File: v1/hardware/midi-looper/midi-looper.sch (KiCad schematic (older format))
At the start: 19 parts

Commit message: Updated schematic
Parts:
- added R? (x3): 10, symbol Device:R
- added R? (x3): 33, symbol Device:R
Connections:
- net +3V3: now also R?.1, R?.1, R?.1
- net GND: now also J?.2 (Pin_2), J?.2 (Pin_2), J?.2 (Pin_2)
- net TX3: now reaches U?.10 (8_TX3_DIN)
- net TX3: now also R?.2
- net TX2: now reaches U?.12 (10_TX2_CS_PWM)
- net TX2: now also R?.2
- net TX1: now reaches U?.3 (1_TX1_Touch)
- net TX1: now also R?.2
- net at J?.1 (Pin_1): now also R?.1 (x3)
- net at J?.3 (Pin_3): now also R?.2 (x3)
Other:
- moved on the sheet: J?
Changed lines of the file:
@@
 L Connector:Conn_01x03_Female J?
 U 1 1 61B8E575
-P 3950 1000
-F 0 "J?" V 3888 812 50  0000 R CNN
-F 1 "Conn_01x03_Female" V 3797 812 50  0000 R CNN
-F 2 "" H 3950 1000 50  0001 C CNN
-F 3 "~" H 3950 1000 50  0001 C CNN
-	1    3950 1000
+P 7550 1400
+F 0 "J?" V 7488 1212 50  0000 R CNN
+F 1 "Conn_01x03_Female" V 7397 1212 50  0000 R CNN
+F 2 "" H 7550 1400 50  0001 C CNN
+F 3 "~" H 7550 1400 50  0001 C CNN
+	1    7550 1400
 	0    -1   -1   0
 $EndComp
@@
 L Connector:Conn_01x03_Female J?
 U 1 1 61B91527
-P 4900 1000
-F 0 "J?" V 4838 812 50  0000 R CNN
-F 1 "Conn_01x03_Female" V 4747 812 50  0000 R CNN
-F 2 "" H 4900 1000 50  0001 C CNN
-F 3 "~" H 4900 1000 50  0001 C CNN
-	1    4900 1000
+P 8500 1400
+F 0 "J?" V 8438 1212 50  0000 R CNN
+F 1 "Conn_01x03_Female" V 8347 1212 50  0000 R CNN
+F 2 "" H 8500 1400 50  0001 C CNN
+F 3 "~" H 8500 1400 50  0001 C CNN
+	1    8500 1400
 	0    -1   -1   0
 $EndComp
@@
 L Connector:Conn_01x03_Female J?
 U 1 1 61B91E09
-P 5850 1000
-F 0 "J?" V 5788 812 50  0000 R CNN
-F 1 "Conn_01x03_Female" V 5697 812 50  0000 R CNN
-F 2 "" H 5850 1000 50  0001 C CNN
-F 3 "~" H 5850 1000 50  0001 C CNN
-	1    5850 1000
+P 9450 1400
+F 0 "J?" V 9388 1212 50  0000 R CNN
+F 1 "Conn_01x03_Female" V 9297 1212 50  0000 R CNN
+F 2 "" H 9450 1400 50  0001 C CNN
+F 3 "~" H 9450 1400 50  0001 C CNN
+	1    9450 1400
 	0    -1   -1   0
 $EndComp
+$Comp
+L Device:R R?
+U 1 1 61B9C710
+P 7450 1750
+F 0 "R?" H 7520 1796 50  0000 L CNN
+F 1 "10" H 7520 1705 50  0000 L CNN
+F 2 "" V 7380 1750 50  0001 C CNN
+F 3 "~" H 7450 1750 50  0001 C CNN
+	1    7450 1750
+	1    0    0    -1
+$EndComp
+$Comp
+L Device:R R?
+U 1 1 61B9D0B4
+P 8400 1750
+F 0 "R?" H 8470 1796 50  0000 L CNN
+F 1 "10" H 8470 1705 50  0000 L CNN
+F 2 "" V 8330 1750 50  0001 C CNN
+F 3 "~" H 8400 1750 50  0001 C CNN
+	1    8400 1750
+	1    0    0    -1
+$EndComp
+$Comp
+L Device:R R?
+U 1 1 61B9D95C
+P 9350 1750
+F 0 "R?" H 9420 1796 50  0000 L CNN
+F 1 "10" H 9420 1705 50  0000 L CNN
+F 2 "" V 9280 1750 50  0001 C CNN
+F 3 "~" H 9350 1750 50  0001 C CNN
+	1    9350 1750
+	1    0    0    -1
+$EndComp
+Text Label 7450 1900 0    50   ~ 0
+TX1
+Text Label 8400 1900 0    50   ~ 0
+TX2
+Text Label 9350 1900 0    50   ~ 0
+TX3
+Text Label 6000 3950 0    50   ~ 0
+TX1
+Text Label 5100 3950 0    50   ~ 0
+TX2
+Text Label 5300 3950 0    50   ~ 0
+TX3
+$Comp
+L power:GND #PWR?
+U 1 1 61BA81F2
+P 7550 2000
+F 0 "#PWR?" H 7550 1750 50  0001 C CNN
+F 1 "GND" H 7555 1827 50  0000 C CNN
+F 2 "" H 7550 2000 50  0001 C CNN
+F 3 "" H 7550 2000 50  0001 C CNN
+	1    7550 2000
+	1    0    0    -1
+$EndComp
+$Comp
+L power:GND #PWR?
+U 1 1 61BA87AF
+P 8500 1950
+F 0 "#PWR?" H 8500 1700 50  0001 C CNN
+F 1 "GND" H 8505 1777 50  0000 C CNN
+F 2 "" H 8500 1950 50  0001 C CNN
+F 3 "" H 8500 1950 50  0001 C CNN
+	1    8500 1950
+	1    0    0    -1
+$EndComp
+$Comp
+L power:GND #PWR?
+U 1 1 61BA8AF1
+P 9450 1950
+F 0 "#PWR?" H 9450 1700 50  0001 C CNN
+F 1 "GND" H 9455 1777 50  0000 C CNN
+F 2 "" H 9450 1950 50  0001 C CNN
+F 3 "" H 9450 1950 50  0001 C CNN
+	1    9450 1950
+	1    0    0    -1
+$EndComp
+Wire Wire Line
+	9450 1600 9450 1950
+Wire Wire Line
+	8500 1600 8500 1950
+Wire Wire Line
+	7550 2000 7550 1600
+$Comp
+L Device:R R?
+U 1 1 61BAD6A1
+P 9700 1600
+F 0 "R?" V 9493 1600 50  0000 C CNN
+F 1 "33" V 9584 1600 50  0000 C CNN
+F 2 "" V 9630 1600 50  0001 C CNN
+F 3 "~" H 9700 1600 50  0001 C CNN
+	1    9700 1600
+	0    1    1    0
+$EndComp
+$Comp
+L Device:R R?
+U 1 1 61BADCD9
+P 8750 1600
+F 0 "R?" V 8543 1600 50  0000 C CNN
+F 1 "33" V 8634 1600 50  0000 C CNN
+F 2 "" V 8680 1600 50  0001 C CNN
+F 3 "~" H 8750 1600 50  0001 C CNN
+	1    8750 1600
+	0    1    1    0
+$EndComp
+$Comp
+L Device:R R?
+U 1 1 61BAE254
+P 7800 1600
+F 0 "R?" V 7593 1600 50  0000 C CNN
+F 1 "33" V 7684 1600 50  0000 C CNN
+F 2 "" V 7730 1600 50  0001 C CNN
+F 3 "~" H 7800 1600 50  0001 C CNN
+	1    7800 1600
+	0    1    1    0
+$EndComp
+$Comp
+L power:+3.3V #PWR?
+U 1 1 61BAEFCC
+P 9850 1600
+F 0 "#PWR?" H 9850 1450 50  0001 C CNN
+F 1 "+3.3V" V 9865 1728 50  0000 L CNN
+F 2 "" H 9850 1600 50  0001 C CNN
+F 3 "" H 9850 1600 50  0001 C CNN
+	1    9850 1600
+	0    1    1    0
+$EndComp
+$Comp
+L power:+3.3V #PWR?
+U 1 1 61BAF8B9
+P 8900 1600
+F 0 "#PWR?" H 8900 1450 50  0001 C CNN
+F 1 "+3.3V" V 8915 1728 50  0000 L CNN
+F 2 "" H 8900 1600 50  0001 C CNN
+F 3 "" H 8900 1600 50  0001 C CNN
+	1    8900 1600
+	0    1    1    0
+$EndComp
+$Comp
+L power:+3.3V #PWR?
+U 1 1 61BAFE97
+P 7950 1600
+F 0 "#PWR?" H 7950 1450 50  0001 C CNN
+F 1 "+3.3V" V 7965 1728 50  0000 L CNN
+F 2 "" H 7950 1600 50  0001 C CNN
+F 3 "" H 7950 1600 50  0001 C CNN
+	1    7950 1600
+	0    1    1    0
+$EndComp
 $EndSCHEMATC

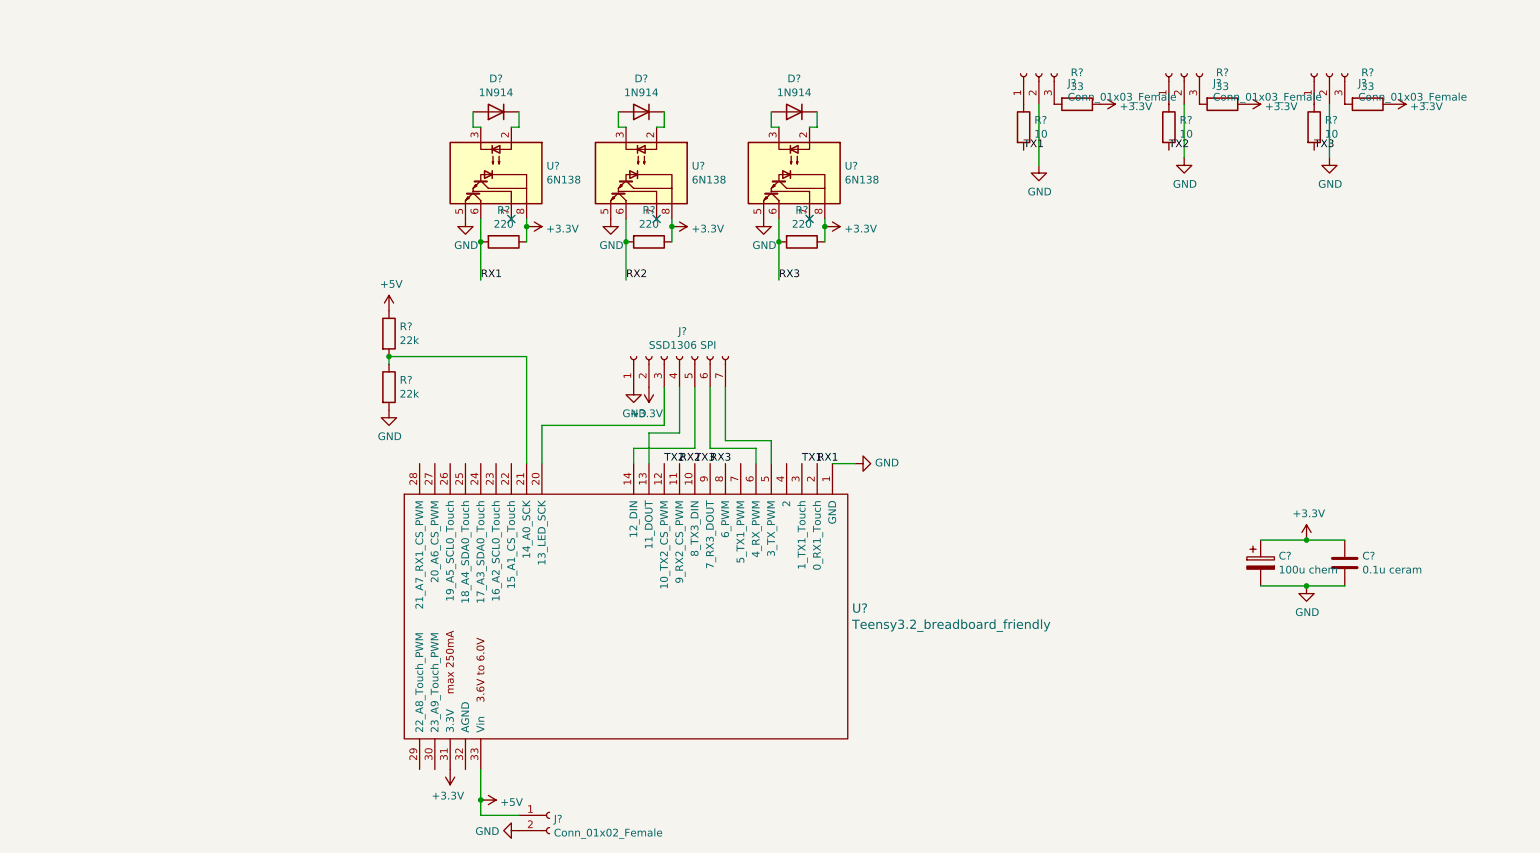
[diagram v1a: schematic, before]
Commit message: Complete initial schematic
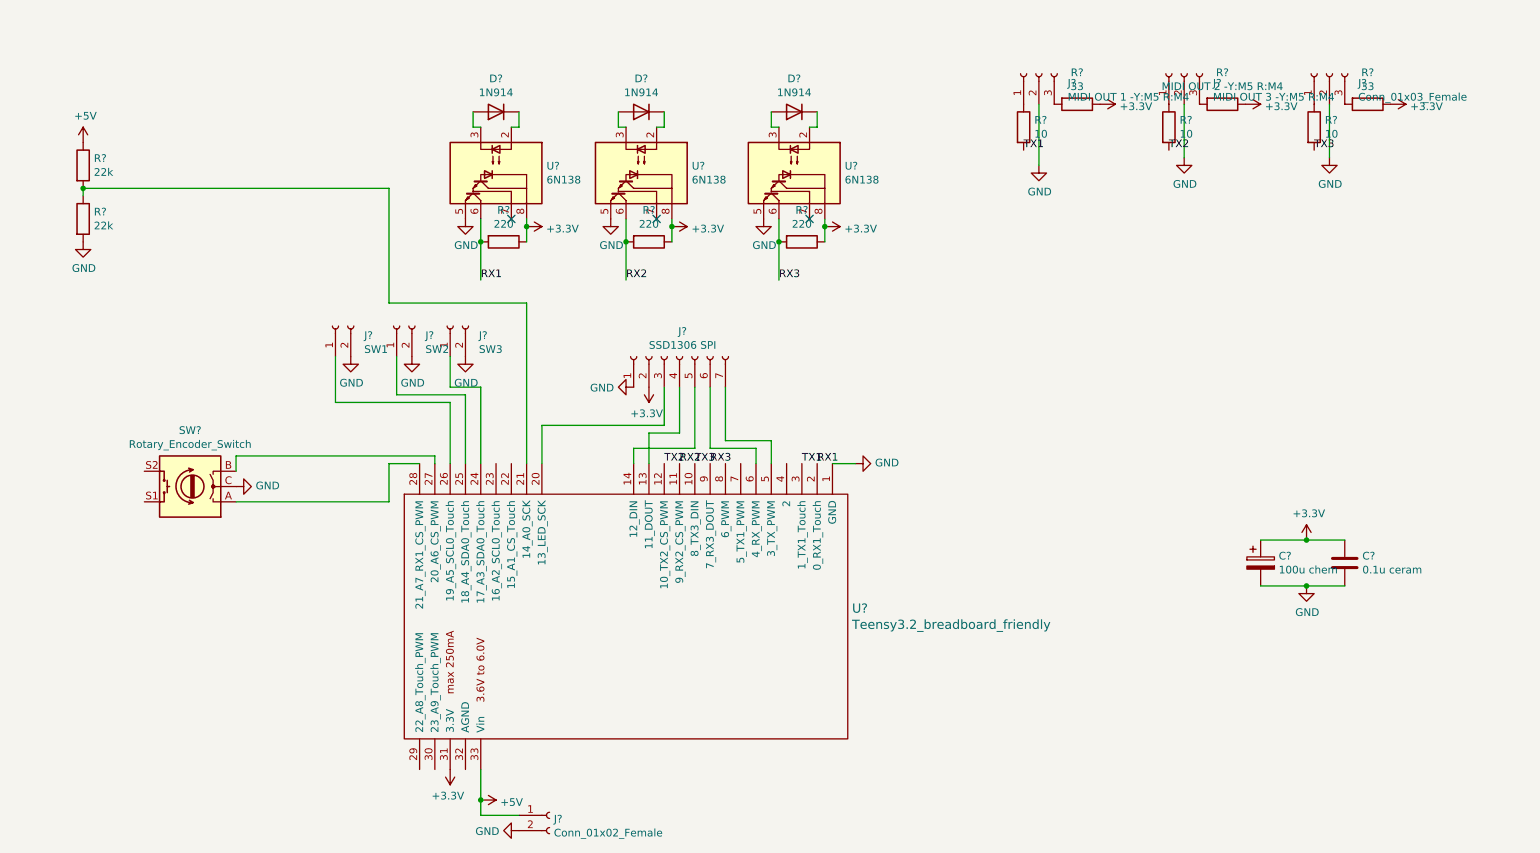
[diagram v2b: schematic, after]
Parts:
- added J?: SW1, symbol Connector:Conn_01x02_Female
- added J?: SW2, symbol Connector:Conn_01x02_Female
- added J?: SW3, symbol Connector:Conn_01x02_Female
- added SW?: Rotary_Encoder_Switch, symbol Device:Rotary_Encoder_Switch
- J?: value Conn_01x03_Female -> MIDI OUT 1 -Y:M5 R:M4
- J?: value Conn_01x03_Female -> MIDI OUT 3 -Y:M5 R:M4
- R?: value 33 -> MIDI OUT 2 -Y:M5 R:M4
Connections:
- net GND: now also J?.2 (Pin_2), J?.2 (Pin_2), J?.2 (Pin_2), SW?.C
- net at U?.24 (17_A3_SDA0_Touch): now also J?.1 (Pin_1)
- net at U?.25 (18_A4_SDA0_Touch): now also J?.1 (Pin_1)
- net at U?.26 (19_A5_SCL0_Touch): now also J?.1 (Pin_1)
- net at U?.27 (20_A6_CS_PWM): now also SW?.B
- net at U?.28 (21_A7_RX1_CS_PWM): now also SW?.A
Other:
- moved on the sheet: R?
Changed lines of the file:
@@
 P 4900 3450
 F 0 "#PWR?" H 4900 3200 50  0001 C CNN
-F 1 "GND" H 4905 3277 50  0000 C CNN
+F 1 "GND" V 4905 3322 50  0000 R CNN
 F 2 "" H 4900 3450 50  0001 C CNN
 F 3 "" H 4900 3450 50  0001 C CNN
 	1    4900 3450
-	1    0    0    -1
+	0    1    1    0
 $EndComp
 $Comp
@@
 	-1   0    0    1
 $EndComp
-Wire Wire Line
-	9000 4450 9300 4450
 $Comp
 L power:+5V #PWR?
 U 1 1 61B75368
-P 3300 2950
-F 0 "#PWR?" H 3300 2800 50  0001 C CNN
-F 1 "+5V" H 3315 3123 50  0000 C CNN
-F 2 "" H 3300 2950 50  0001 C CNN
-F 3 "" H 3300 2950 50  0001 C CNN
-	1    3300 2950
+P 1300 1850
+F 0 "#PWR?" H 1300 1700 50  0001 C CNN
+F 1 "+5V" H 1315 2023 50  0000 C CNN
+F 2 "" H 1300 1850 50  0001 C CNN
+F 3 "" H 1300 1850 50  0001 C CNN
+	1    1300 1850
 	1    0    0    -1
 $EndComp
@@
 L Device:R R?
 U 1 1 61B75E1A
-P 3300 3100
-F 0 "R?" H 3370 3146 50  0000 L CNN
-F 1 "22k" H 3370 3055 50  0000 L CNN
-F 2 "" V 3230 3100 50  0001 C CNN
-F 3 "~" H 3300 3100 50  0001 C CNN
-	1    3300 3100
+P 1300 2000
+F 0 "R?" H 1370 2046 50  0000 L CNN
+F 1 "22k" H 1370 1955 50  0000 L CNN
+F 2 "" V 1230 2000 50  0001 C CNN
+F 3 "~" H 1300 2000 50  0001 C CNN
+	1    1300 2000
 	1    0    0    -1
 $EndComp
@@
 L Device:R R?
 U 1 1 61B7670C
-P 3300 3450
-F 0 "R?" H 3370 3496 50  0000 L CNN
-F 1 "22k" H 3370 3405 50  0000 L CNN
-F 2 "" V 3230 3450 50  0001 C CNN
-F 3 "~" H 3300 3450 50  0001 C CNN
-	1    3300 3450
+P 1300 2350
+F 0 "R?" H 1370 2396 50  0000 L CNN
+F 1 "22k" H 1370 2305 50  0000 L CNN
+F 2 "" V 1230 2350 50  0001 C CNN
+F 3 "~" H 1300 2350 50  0001 C CNN
+	1    1300 2350
 	1    0    0    -1
 $EndComp
@@
 L power:GND #PWR?
 U 1 1 61B76E07
-P 3300 3600
-F 0 "#PWR?" H 3300 3350 50  0001 C CNN
-F 1 "GND" H 3305 3427 50  0000 C CNN
-F 2 "" H 3300 3600 50  0001 C CNN
-F 3 "" H 3300 3600 50  0001 C CNN
-	1    3300 3600
-	1    0    0    -1
-$EndComp
-Wire Wire Line
-	3300 3250 3300 3300
-Wire Wire Line
-	4200 3950 4200 3250
-Wire Wire Line
-	4200 3250 3300 3250
-Connection ~ 3300 3250
+P 1300 2500
+F 0 "#PWR?" H 1300 2250 50  0001 C CNN
+F 1 "GND" H 1305 2327 50  0000 C CNN
+F 2 "" H 1300 2500 50  0001 C CNN
+F 3 "" H 1300 2500 50  0001 C CNN
+	1    1300 2500
+	1    0    0    -1
+$EndComp
+Wire Wire Line
+	1300 2150 1300 2200
+Connection ~ 1300 2150
 $Comp
 L Connector:Conn_01x03_Female J?
@@
 P 7550 1400
 F 0 "J?" V 7488 1212 50  0000 R CNN
-F 1 "Conn_01x03_Female" V 7397 1212 50  0000 R CNN
+F 1 "MIDI OUT 1 -Y:M5 R:M4" V 7397 1212 50  0000 R CNN
 F 2 "" H 7550 1400 50  0001 C CNN
 F 3 "~" H 7550 1400 50  0001 C CNN
@@
 P 8500 1400
 F 0 "J?" V 8438 1212 50  0000 R CNN
-F 1 "Conn_01x03_Female" V 8347 1212 50  0000 R CNN
+F 1 "MIDI OUT 3 -Y:M5 R:M4" V 8347 1212 50  0000 R CNN
 F 2 "" H 8500 1400 50  0001 C CNN
 F 3 "~" H 8500 1400 50  0001 C CNN
@@
 P 8750 1600
 F 0 "R?" V 8543 1600 50  0000 C CNN
-F 1 "33" V 8634 1600 50  0000 C CNN
+F 1 "MIDI OUT 2 -Y:M5 R:M4" V 8634 1600 50  0000 C CNN
 F 2 "" V 8680 1600 50  0001 C CNN
 F 3 "~" H 8750 1600 50  0001 C CNN
@@
 	0    1    1    0
 $EndComp
+Wire Wire Line
+	9000 4450 9300 4450
+$Comp
+L Device:Rotary_Encoder_Switch SW?
+U 1 1 61BBEB55
+P 2000 4100
+F 0 "SW?" H 2000 3733 50  0000 C CNN
+F 1 "Rotary_Encoder_Switch" H 2000 3824 50  0000 C CNN
+F 2 "" H 1850 4260 50  0001 C CNN
+F 3 "~" H 2000 4360 50  0001 C CNN
+	1    2000 4100
+	-1   0    0    1
+$EndComp
+$Comp
+L power:GND #PWR?
+U 1 1 61BC1206
+P 2300 4100
+F 0 "#PWR?" H 2300 3850 50  0001 C CNN
+F 1 "GND" V 2305 3972 50  0000 R CNN
+F 2 "" H 2300 4100 50  0001 C CNN
+F 3 "" H 2300 4100 50  0001 C CNN
+	1    2300 4100
+	0    -1   -1   0
+$EndComp
+Wire Wire Line
+	2300 4200 3300 4200
+Wire Wire Line
+	3300 4200 3300 3950
+Wire Wire Line
+	3300 3950 3500 3950
+Wire Wire Line
+	3600 3950 3600 3900
+Wire Wire Line
+	3600 3900 2300 3900
+Wire Wire Line
+	2300 3900 2300 4000
+Wire Wire Line
+	4200 2900 3300 2900
+Wire Wire Line
+	3300 2900 3300 2150
+Wire Wire Line
+	4200 2900 4200 3950
+Wire Wire Line
+	1300 2150 3300 2150
+$Comp
+L Connector:Conn_01x02_Female J?
+U 1 1 61BDE879
+P 2950 3050
+F 0 "J?" V 2888 2862 50  0000 R CNN
+F 1 "SW1" V 2797 2862 50  0000 R CNN
+F 2 "" H 2950 3050 50  0001 C CNN
+F 3 "~" H 2950 3050 50  0001 C CNN
+	1    2950 3050
+	0    -1   -1   0
+$EndComp
+$Comp
+L Connector:Conn_01x02_Female J?
+U 1 1 61BDF6EB
+P 3350 3050
+F 0 "J?" V 3288 2862 50  0000 R CNN
+F 1 "SW2" V 3197 2862 50  0000 R CNN
+F 2 "" H 3350 3050 50  0001 C CNN
+F 3 "~" H 3350 3050 50  0001 C CNN
+	1    3350 3050
+	0    -1   -1   0
+$EndComp
+$Comp
+L Connector:Conn_01x02_Female J?
+U 1 1 61BE0034
+P 3700 3050
+F 0 "J?" V 3638 2862 50  0000 R CNN
+F 1 "SW3" V 3547 2862 50  0000 R CNN
+F 2 "" H 3700 3050 50  0001 C CNN
+F 3 "~" H 3700 3050 50  0001 C CNN
+	1    3700 3050
+	0    -1   -1   0
+$EndComp
+$Comp
+L power:GND #PWR?
+U 1 1 61BE421A
+P 3050 3250
+F 0 "#PWR?" H 3050 3000 50  0001 C CNN
+F 1 "GND" H 3055 3077 50  0000 C CNN
+F 2 "" H 3050 3250 50  0001 C CNN
+F 3 "" H 3050 3250 50  0001 C CNN
+	1    3050 3250
+	1    0    0    -1
+$EndComp
+$Comp
+L power:GND #PWR?
+U 1 1 61BE4AA7
+P 3450 3250
+F 0 "#PWR?" H 3450 3000 50  0001 C CNN
+F 1 "GND" H 3455 3077 50  0000 C CNN
+F 2 "" H 3450 3250 50  0001 C CNN
+F 3 "" H 3450 3250 50  0001 C CNN
+	1    3450 3250
+	1    0    0    -1
+$EndComp
+$Comp
+L power:GND #PWR?
+U 1 1 61BE94B9
+P 3800 3250
+F 0 "#PWR?" H 3800 3000 50  0001 C CNN
+F 1 "GND" H 3805 3077 50  0000 C CNN
+F 2 "" H 3800 3250 50  0001 C CNN
+F 3 "" H 3800 3250 50  0001 C CNN
+	1    3800 3250
+	1    0    0    -1
+$EndComp
+Wire Wire Line
+	2950 3250 2950 3550
+Wire Wire Line
+	2950 3550 3700 3550
+Wire Wire Line
+	3700 3550 3700 3950
+Wire Wire Line
+	3800 3950 3800 3500
+Wire Wire Line
+	3800 3500 3350 3500
+Wire Wire Line
+	3350 3500 3350 3250
+Wire Wire Line
+	3700 3250 3700 3450
+Wire Wire Line
+	3700 3450 3900 3450
+Wire Wire Line
+	3900 3450 3900 3950
 $EndSCHEMATC

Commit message: Added net - assigned components
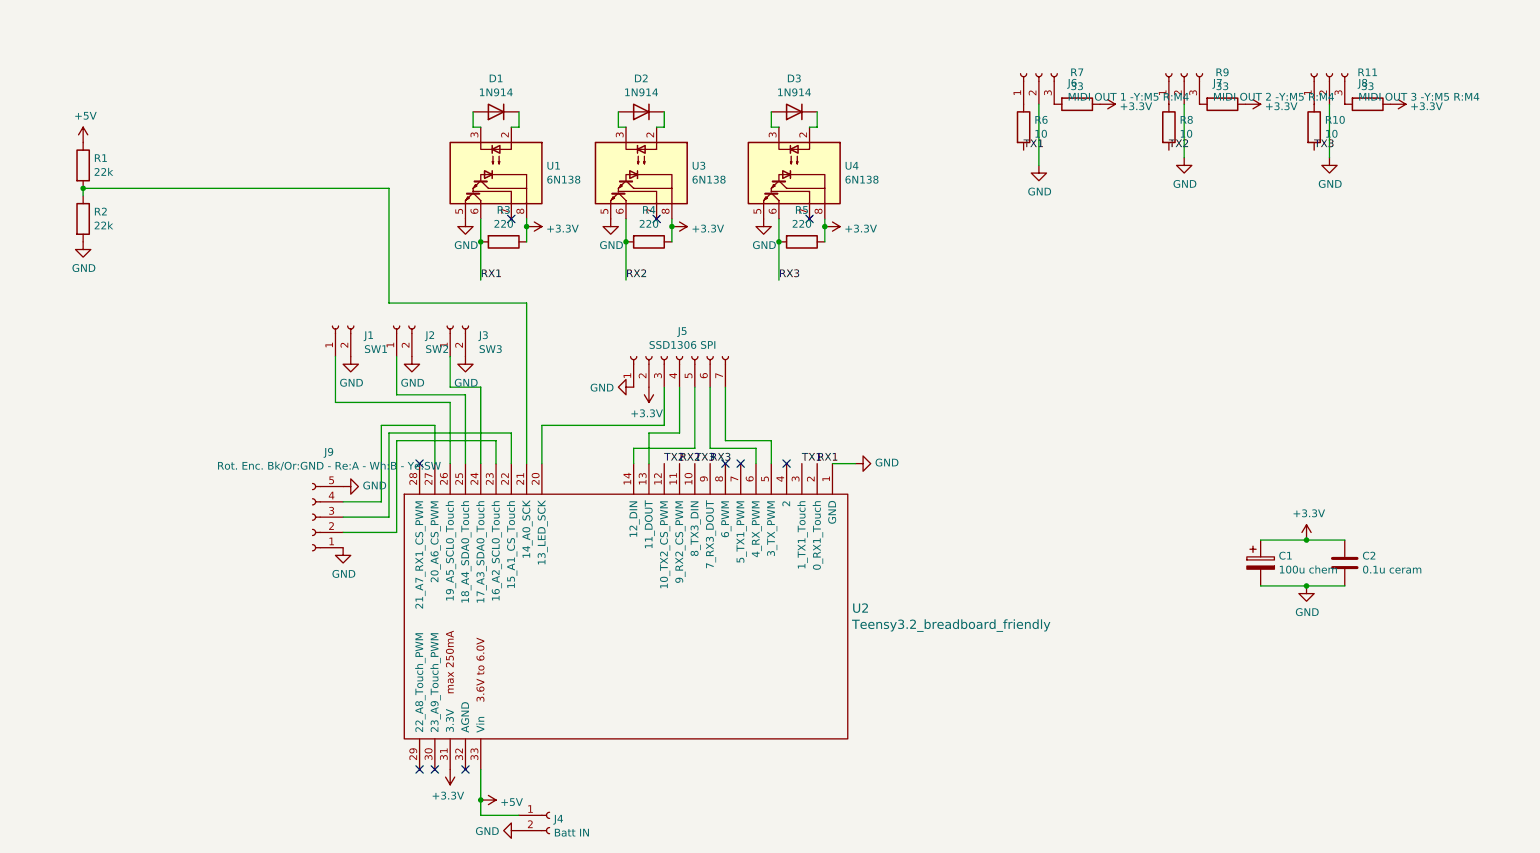
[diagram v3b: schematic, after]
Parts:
- removed SW?: Rotary_Encoder_Switch, symbol Device:Rotary_Encoder_Switch
- added J9: Rot. Enc. Bk/Or:GND - Re:A - Wh:B - Ye:SW, Connector_JST:JST_EH_B5B-EH-A_1x05_P2.50mm_Vertical, symbol Connector:Conn_01x05_Female
- C1: renamed from C?; footprint (none) -> Capacitor_THT:CP_Radial_D5.0mm_P2.50mm
- C2: renamed from C?; footprint (none) -> Capacitor_THT:C_Axial_L3.8mm_D2.6mm_P7.50mm_Horizontal
- J1, J2, J3: renamed from J?; footprint (none) -> Connector_JST:JST_EH_B2B-EH-A_1x02_P2.50mm_Vertical
- J4: renamed from J?; value Conn_01x02_Female -> Batt IN; footprint (none) -> Connector_JST:JST_EH_B2B-EH-A_1x02_P2.50mm_Vertical
- J5: renamed from J?; footprint (none) -> Connector_JST:JST_EH_B7B-EH-A_1x07_P2.50mm_Vertical
- J6: renamed from J?; footprint (none) -> Connector_JST:JST_EH_B3B-EH-A_1x03_P2.50mm_Vertical
- J7: renamed from J?; value MIDI OUT 3 -Y:M5 R:M4 -> MIDI OUT 2 -Y:M5 R:M4; footprint (none) -> Connector_JST:JST_EH_B3B-EH-A_1x03_P2.50mm_Vertical
- J8: renamed from J?; value Conn_01x03_Female -> MIDI OUT 3 -Y:M5 R:M4; footprint (none) -> Connector_JST:JST_EH_B3B-EH-A_1x03_P2.50mm_Vertical
- R1, R10, R11, R2, R3, R4, R5, R6, R7, R8: renamed from R?; footprint (none) -> Resistor_THT:R_Axial_DIN0207_L6.3mm_D2.5mm_P7.62mm_Horizontal
- R9: renamed from R?; value MIDI OUT 2 -Y:M5 R:M4 -> 33; footprint (none) -> Resistor_THT:R_Axial_DIN0207_L6.3mm_D2.5mm_P7.62mm_Horizontal
- U1, U3, U4: renamed from U?; footprint (none) -> Package_DIP:DIP-8_W7.62mm_LongPads
- U2: renamed from U?; footprint (none) -> teensy:Teensy30_31_32_breadboard_friendly
- gave numbers to parts that had none: 3
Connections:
- net GND: now also J9.1 (Pin_1), J9.5 (Pin_5)
- net at U2.22 (15_A1_CS_Touch): now also J9.3 (Pin_3)
- net at U2.23 (16_A2_SCL0_Touch): now also J9.2 (Pin_2)
- net at U2.27 (20_A6_CS_PWM): now also J9.4 (Pin_4)
- no-connect marks 3 -> 10
